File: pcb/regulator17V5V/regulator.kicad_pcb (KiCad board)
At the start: 2 copper layers, 10 x 16.5 mm, 8 parts, among them J1 Conn_01x05_Socket, J2 Conn_01x05_Socket, J3 Conn_01x02, U1 TPS82130

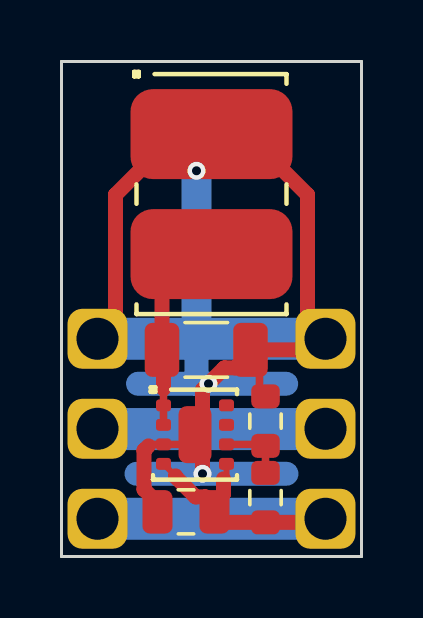
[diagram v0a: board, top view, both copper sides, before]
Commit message: Use ISL3280E
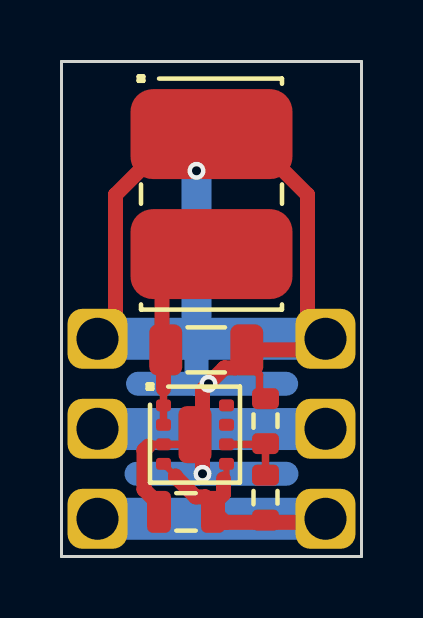
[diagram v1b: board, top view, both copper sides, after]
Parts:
- C1: footprint Capacitor_SMD:C_1206_3216Metric -> local:1206
- C2: footprint Capacitor_SMD:C_0805_2012Metric -> local:0805
- R1, R2: footprint Resistor_SMD:R_0603_1608Metric -> local:0603
- turned U1 to 0 degrees
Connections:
- net +15V renamed +12V
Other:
- board text added: "LED Strip"

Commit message: New pin ordering for Harting connector
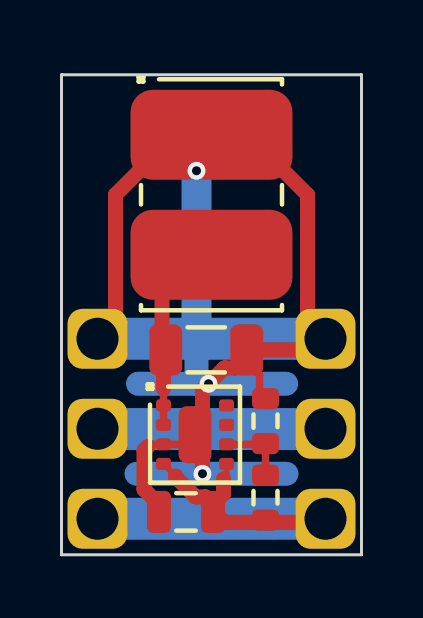
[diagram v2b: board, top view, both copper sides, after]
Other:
- board size 10 x 16.5 mm -> 10 x 16 mm
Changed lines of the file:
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@@
 			(at 0 0 90)
 			(layer "F.Fab")
+			(hide yes)
 			(effects
 				(font
@@
 		(descr "Texas Instruments buck converter (https://www.ti.com/product/de-de/TPS82130)")
 		(property "Reference" "U1"
-			(at 0 0 360)
+			(at 0 0 0)
 			(layer "F.SilkS")
 			(hide yes)
@@
 		)
 		(property "Value" "TPS82130"
-			(at 0 0 360)
+			(at 0 0 0)
 			(layer "F.Fab")
 			(effects
@@
 			(at 0 0 90)
 			(layer "F.Fab")
+			(hide yes)
 			(effects
 				(font
@@
 	(footprint "local:Kyocera-009176002001906"
 		(layer "F.Cu")
-		(at 135 97.1775 -90)
+		(at 135 97.2 -90)
 		(descr "Kyocera IDC 2 positions 0.8mm² / 18 AWG (https://datasheets.kyocera-avx.com/StandardIDC_00-9176.pdf)")
 		(property "Reference" "J3"
@@
 	)
 	(gr_rect
-		(start 130 92.7575)
-		(end 140 109.2575)
+		(start 130 93.2)
+		(end 140 109.2)
 		(stroke
 			(width 0.1)
